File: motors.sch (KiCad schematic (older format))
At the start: 24 parts, among them M1 ALIS-CUSTOM-PARTS_POWERPADS, M2 ALIS-CUSTOM-PARTS_POWERPADS, M3 ALIS-CUSTOM-PARTS_POWERPADS, M4 ALIS-CUSTOM-PARTS_POWERPADS, M5 ALIS-CUSTOM-PARTS_POWERPADS, Q2 BSS138, Q3 BSS138, Q4 BSS138, Q5 BSS138, Q6 BSS138

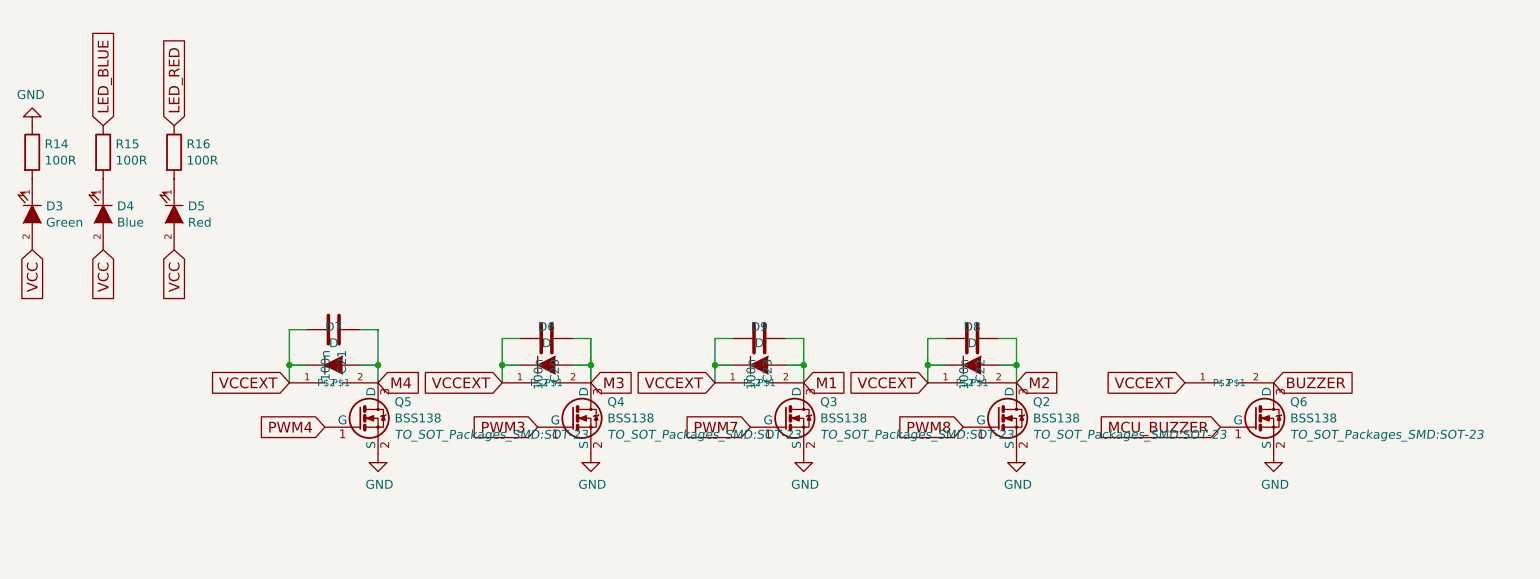
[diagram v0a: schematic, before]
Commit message: changed some netnames
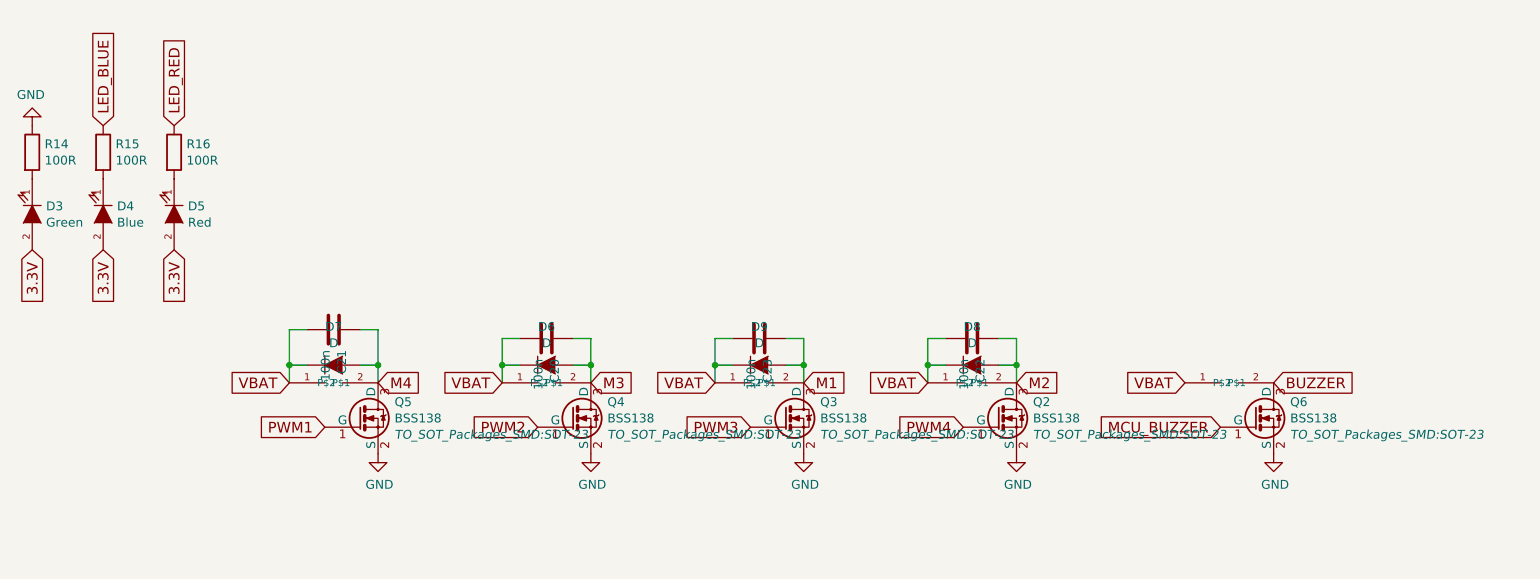
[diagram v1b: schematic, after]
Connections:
- net PWM7 is gone; now on net PWM3: Q3.1 (G)
- net PWM8 is gone; now on net PWM4: Q2.1 (G)
- net PWM3: no longer Q4.1 (G)
- net PWM4: no longer Q5.1 (G)
- net VCC renamed 3.3V
- net VCCEXT renamed VBAT
- new net PWM1: Q5.1 (G)
- new net PWM2: Q4.1 (G)
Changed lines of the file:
@@
 BUZZER
 $Comp
-L GND #PWR21
+L GND #PWR010
 U 1 1 569BDE16
 P 8200 3350
-F 0 "#PWR21" H 8200 3100 50  0001 C CNN
+F 0 "#PWR010" H 8200 3100 50  0001 C CNN
 F 1 "GND" H 8208 3176 50  0000 C CNN
 F 2 "" H 8200 3350 50  0000 C CNN
@@
 MCU_BUZZER
 Text GLabel 7700 2950 0    60   Input ~ 0
-VCCEXT
+VBAT
 $Comp
 L ALIS-CUSTOM-PARTS_POWERPADS M?
@@
 $EndComp
 $Comp
-L GND #PWR19
+L GND #PWR011
 U 1 1 569BDE42
 P 5550 3350
-F 0 "#PWR19" H 5550 3100 50  0001 C CNN
+F 0 "#PWR011" H 5550 3100 50  0001 C CNN
 F 1 "GND" H 5558 3176 50  0000 C CNN
 F 2 "" H 5550 3350 50  0000 C CNN
@@
 $EndComp
 Text GLabel 5050 2950 0    60   Input ~ 0
-VCCEXT
+VBAT
 $Comp
 L ALIS-CUSTOM-PARTS_POWERPADS M?
@@
 $EndComp
 Text GLabel 5250 3200 0    60   Input ~ 0
-PWM7
+PWM3
 $Comp
 L BSS138 Q2
@@
 $EndComp
 Text GLabel 6250 2950 0    60   Input ~ 0
-VCCEXT
+VBAT
 Text GLabel 6450 3200 0    60   Input ~ 0
-PWM8
+PWM4
 $Comp
 L BSS138 Q4
@@
 $EndComp
 Text GLabel 3850 2950 0    60   Input ~ 0
-VCCEXT
+VBAT
 Text GLabel 4050 3200 0    60   Input ~ 0
-PWM3
-$Comp
-L GND #PWR16
+PWM2
+$Comp
+L GND #PWR012
 U 1 1 569BDE75
 P 4350 3350
-F 0 "#PWR16" H 4350 3100 50  0001 C CNN
+F 0 "#PWR012" H 4350 3100 50  0001 C CNN
 F 1 "GND" H 4358 3176 50  0000 C CNN
 F 2 "" H 4350 3350 50  0000 C CNN
@@
 $EndComp
 Text GLabel 2650 2950 0    60   Input ~ 0
-VCCEXT
+VBAT
 Text GLabel 2850 3200 0    60   Input ~ 0
-PWM4
-$Comp
-L GND #PWR17
+PWM1
+$Comp
+L GND #PWR013
 U 1 1 569BDE8A
 P 3150 3350
-F 0 "#PWR17" H 3150 3100 50  0001 C CNN
+F 0 "#PWR013" H 3150 3100 50  0001 C CNN
 F 1 "GND" H 3158 3176 50  0000 C CNN
 F 2 "" H 3150 3350 50  0000 C CNN
@@
 $EndComp
 $Comp
-L GND #PWR18
+L GND #PWR014
 U 1 1 569BDE90
 P 6750 3350
-F 0 "#PWR18" H 6750 3100 50  0001 C CNN
+F 0 "#PWR014" H 6750 3100 50  0001 C CNN
 F 1 "GND" H 6758 3176 50  0000 C CNN
 F 2 "" H 6750 3350 50  0000 C CNN
@@
 $EndComp
 Text GLabel 2000 2200 3    60   Input ~ 0
-VCC
+3.3V
 Text GLabel 1600 2200 3    60   Input ~ 0
-VCC
-$Comp
-L GND #PWR2
+3.3V
+$Comp
+L GND #PWR015
 U 1 1 569BFFAD
 P 1200 1500
-F 0 "#PWR2" H 1200 1250 50  0001 C CNN
+F 0 "#PWR015" H 1200 1250 50  0001 C CNN
 F 1 "GND" H 1208 1326 50  0000 C CNN
 F 2 "" H 1200 1500 50  0000 C CNN
@@
 $EndComp
 Text GLabel 1200 2200 3    60   Input ~ 0
-VCC
+3.3V
 Text GLabel 2000 1500 1    60   Input ~ 0
 LED_RED

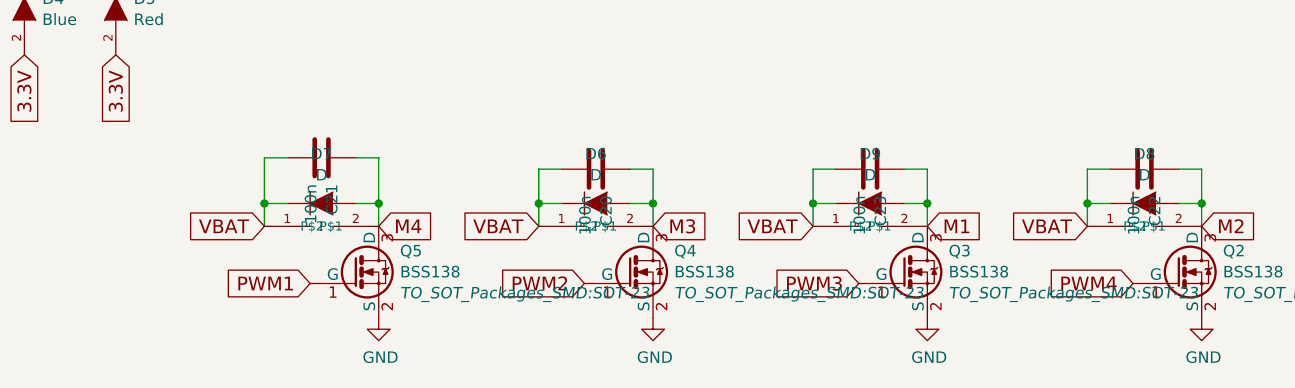
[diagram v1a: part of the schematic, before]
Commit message: OSD running on breadboard
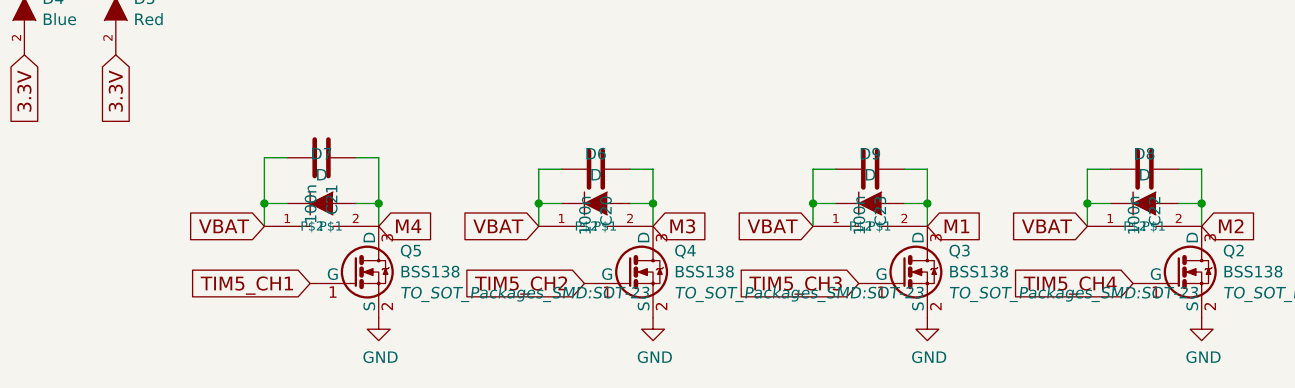
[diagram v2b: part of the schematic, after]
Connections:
- net PWM1 renamed TIM5_CH1
- net PWM2 renamed TIM5_CH2
- net PWM3 renamed TIM5_CH3
- net PWM4 renamed TIM5_CH4
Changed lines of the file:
@@
 BUZZER
 $Comp
-L GND #PWR010
+L GND #PWR014
 U 1 1 569BDE16
 P 8200 3350
-F 0 "#PWR010" H 8200 3100 50  0001 C CNN
+F 0 "#PWR014" H 8200 3100 50  0001 C CNN
 F 1 "GND" H 8208 3176 50  0000 C CNN
 F 2 "" H 8200 3350 50  0000 C CNN
@@
 $EndComp
 $Comp
-L GND #PWR011
+L GND #PWR015
 U 1 1 569BDE42
 P 5550 3350
-F 0 "#PWR011" H 5550 3100 50  0001 C CNN
+F 0 "#PWR015" H 5550 3100 50  0001 C CNN
 F 1 "GND" H 5558 3176 50  0000 C CNN
 F 2 "" H 5550 3350 50  0000 C CNN
@@
 $EndComp
 Text GLabel 5250 3200 0    60   Input ~ 0
-PWM3
+TIM5_CH3
 $Comp
 L BSS138 Q2
@@
 VBAT
 Text GLabel 6450 3200 0    60   Input ~ 0
-PWM4
+TIM5_CH4
 $Comp
 L BSS138 Q4
@@
 VBAT
 Text GLabel 4050 3200 0    60   Input ~ 0
-PWM2
-$Comp
-L GND #PWR012
+TIM5_CH2
+$Comp
+L GND #PWR016
 U 1 1 569BDE75
 P 4350 3350
-F 0 "#PWR012" H 4350 3100 50  0001 C CNN
+F 0 "#PWR016" H 4350 3100 50  0001 C CNN
 F 1 "GND" H 4358 3176 50  0000 C CNN
 F 2 "" H 4350 3350 50  0000 C CNN
@@
 VBAT
 Text GLabel 2850 3200 0    60   Input ~ 0
-PWM1
-$Comp
-L GND #PWR013
+TIM5_CH1
+$Comp
+L GND #PWR017
 U 1 1 569BDE8A
 P 3150 3350
-F 0 "#PWR013" H 3150 3100 50  0001 C CNN
+F 0 "#PWR017" H 3150 3100 50  0001 C CNN
 F 1 "GND" H 3158 3176 50  0000 C CNN
 F 2 "" H 3150 3350 50  0000 C CNN
@@
 $EndComp
 $Comp
-L GND #PWR014
+L GND #PWR018
 U 1 1 569BDE90
 P 6750 3350
-F 0 "#PWR014" H 6750 3100 50  0001 C CNN
+F 0 "#PWR018" H 6750 3100 50  0001 C CNN
 F 1 "GND" H 6758 3176 50  0000 C CNN
 F 2 "" H 6750 3350 50  0000 C CNN
@@
 3.3V
 $Comp
-L GND #PWR015
+L GND #PWR019
 U 1 1 569BFFAD
 P 1200 1500
-F 0 "#PWR015" H 1200 1250 50  0001 C CNN
+F 0 "#PWR019" H 1200 1250 50  0001 C CNN
 F 1 "GND" H 1208 1326 50  0000 C CNN
 F 2 "" H 1200 1500 50  0000 C CNN

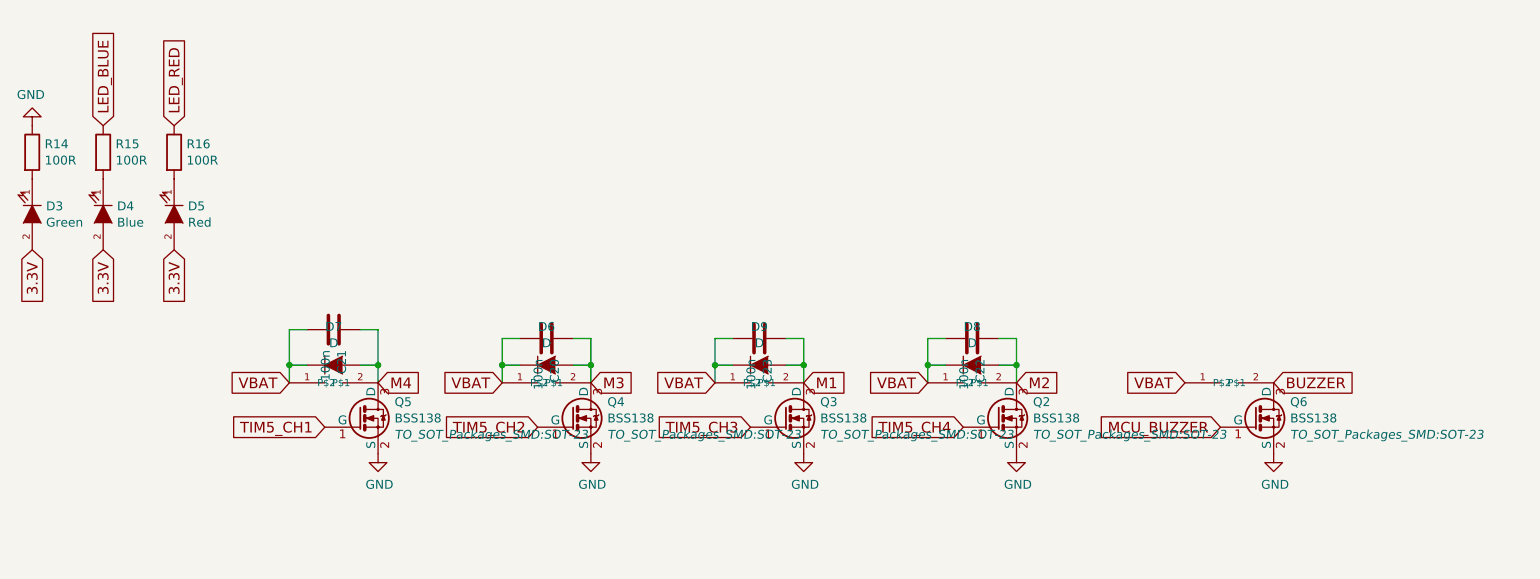
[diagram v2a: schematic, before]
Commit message: power traces routed
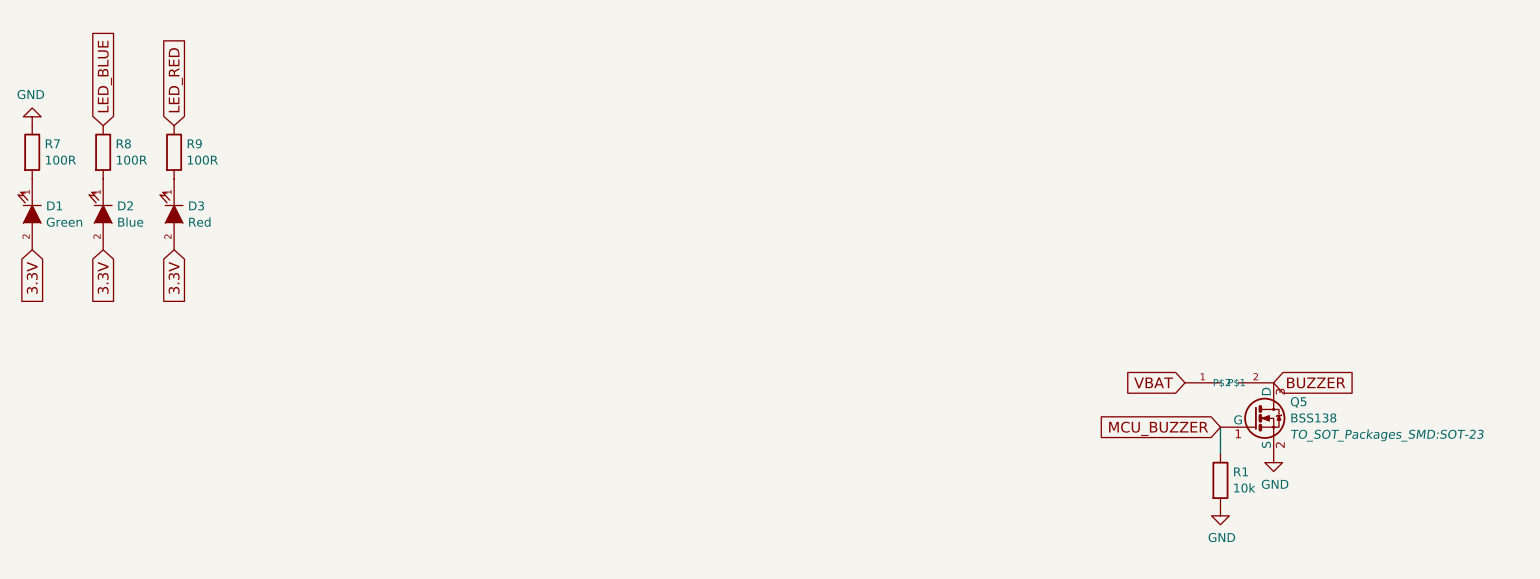
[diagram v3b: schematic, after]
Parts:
- removed C20, C21, C22, C23: 100n, Capacitors_SMD:C_0402, symbol C
- removed D6, D7, D8, D9: D, Diodes_SMD:SOD-323, symbol D
- removed M1, M2, M3, M4: ALIS-CUSTOM-PARTS_POWERPADS, minimal:ALIS-CUSTOM-PARTS_PAD-JUMPER-2-NO_YES_SILK, symbol ALIS-CUSTOM-PARTS_POWERPADS
- removed Q2, Q3, Q4, Q5: BSS138, TO_SOT_Packages_SMD:SOT-23, symbol BSS138
- added R1: 10k, Resistors_SMD:R_0603, symbol R
- R7: renamed from R14; footprint Resistors_SMD:R_0402 -> Resistors_SMD:R_0603
- R8: renamed from R15; footprint Resistors_SMD:R_0402 -> Resistors_SMD:R_0603
- R9: renamed from R16; footprint Resistors_SMD:R_0402 -> Resistors_SMD:R_0603
- renumbered D3 to D1, D4 to D2, D5 to D3, Q6 to Q5
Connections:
- net GND: now also R1.2
- net MCU_BUZZER: now also R1.1
